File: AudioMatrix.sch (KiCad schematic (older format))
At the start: 124 parts, among them J1 AMP3, J2 AMP1, J3 AMP2, J4 Audio In, J5 3V3, J6 5V, J7 GND, J8 IO, J9 ESP, U1 PT2258, U2 PT2258, U3 PT2258, U4 PCA9555PW, U5 MT8816AE1, U6 ESP32-DEVKITC-32D, U7 TPS60403DBVR

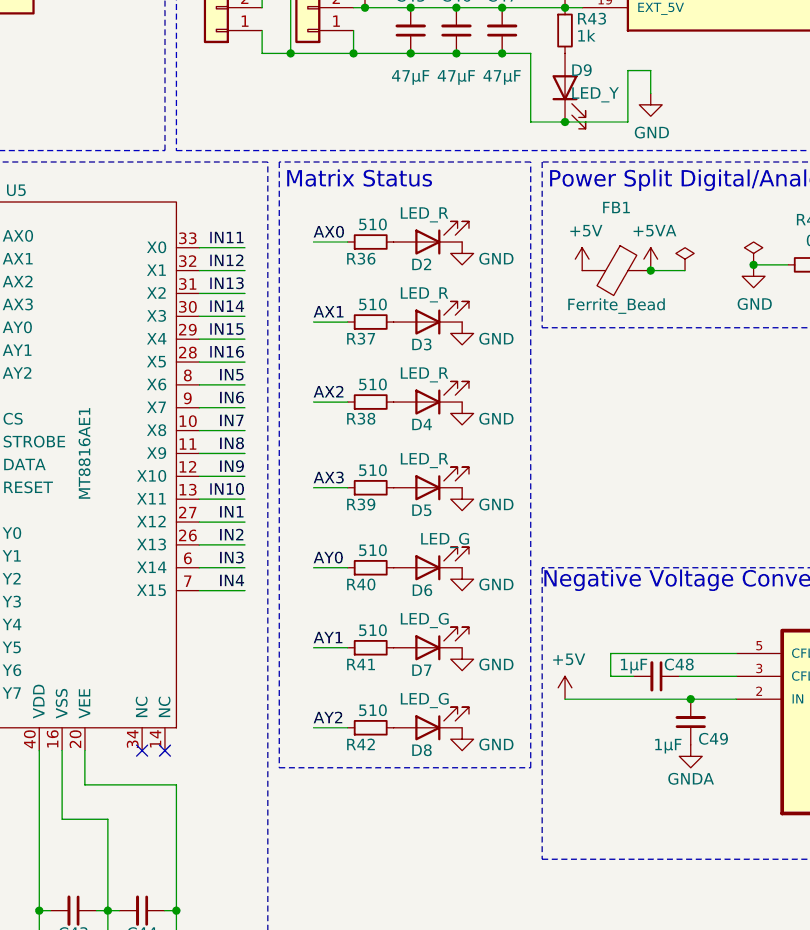
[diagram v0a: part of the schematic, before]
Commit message: Removed LEDs
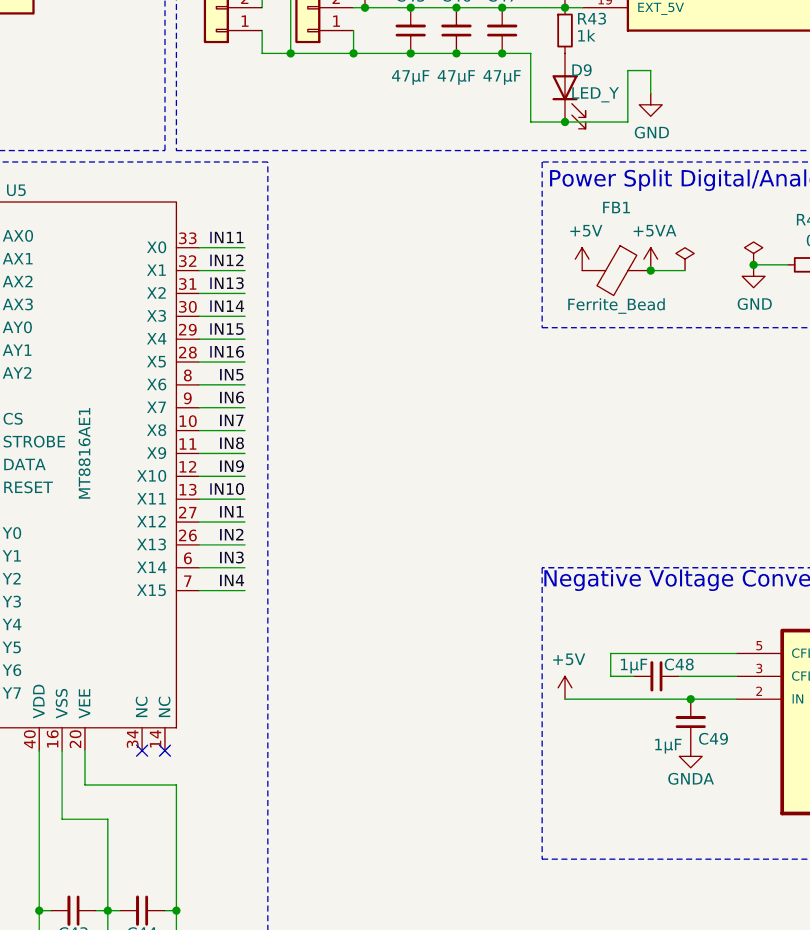
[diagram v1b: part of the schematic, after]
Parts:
- removed D2, D3, D4, D5: LED_R, Diode_SMD:D_0603_1608Metric, symbol Device:LED
- removed D6, D7, D8: LED_G, Diode_SMD:D_0603_1608Metric, symbol Device:LED
- removed R36, R37, R38, R39, R40, R41, R42: 510, Resistor_SMD:R_0603_1608Metric, symbol Device:R_Small
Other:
- note removed: "Matrix Status"

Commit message: Replaced IO expander
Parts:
- removed U4: PCA9555PW, Package_SO:TSSOP-24_4.4x7.8mm_P0.65mm, symbol Interface_Expansion:PCA9555PW
- added R36, R37: 100k, Resistor_SMD:R_0603_1608Metric, symbol Device:R_Small
- added U4: TCA6416APWR, SOP65P640X120-24N, symbol TCA6416APWR:TCA6416APWR
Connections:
- net +5V: now also U4.24 (VCCP)
- net GND: now also C42.2, U4.12 (GND), U4.21 (ADDR); no longer C42.1
- net IO0_0: now also U4.4 (P00)
- net IO0_1: now also U4.5 (P01)
- net IO0_2: now also U4.6 (P02)
- net IO0_3: now also U4.7 (P03)
- net IO0_4: now also U4.8 (P04)
- net IO0_5: now also U4.9 (P05)
- net IO0_6: now also U4.10 (P06)
- net IO0_7: now also U4.11 (P07)
- net IO1_0: now also U4.13 (P10)
- net IO1_1: now also U4.14 (P11)
- net IO1_2: now also U4.15 (P12)
- net IO1_3: now also U4.16 (P13)
- net IO1_4: now also U4.17 (P14)
- net IO1_5: now also U4.18 (P15)
- net IO1_6: now also U4.19 (P16)
- net IO1_7: now also U4.20 (P17)
- net SCL: now also U4.22 (SCL)
- net SDA: now also U4.23 (SDA)
- net 3V3 renamed +3V3
- net +3V3: now also C42.1, R36.1, R37.2, U4.2 (VCC1); no longer C42.2
- new net: R37.1, U4.1 (~INT)
- new net: R36.2, U4.3 (~RESET)
- no-connect marks 15 -> 14
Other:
- moved on the sheet: C42

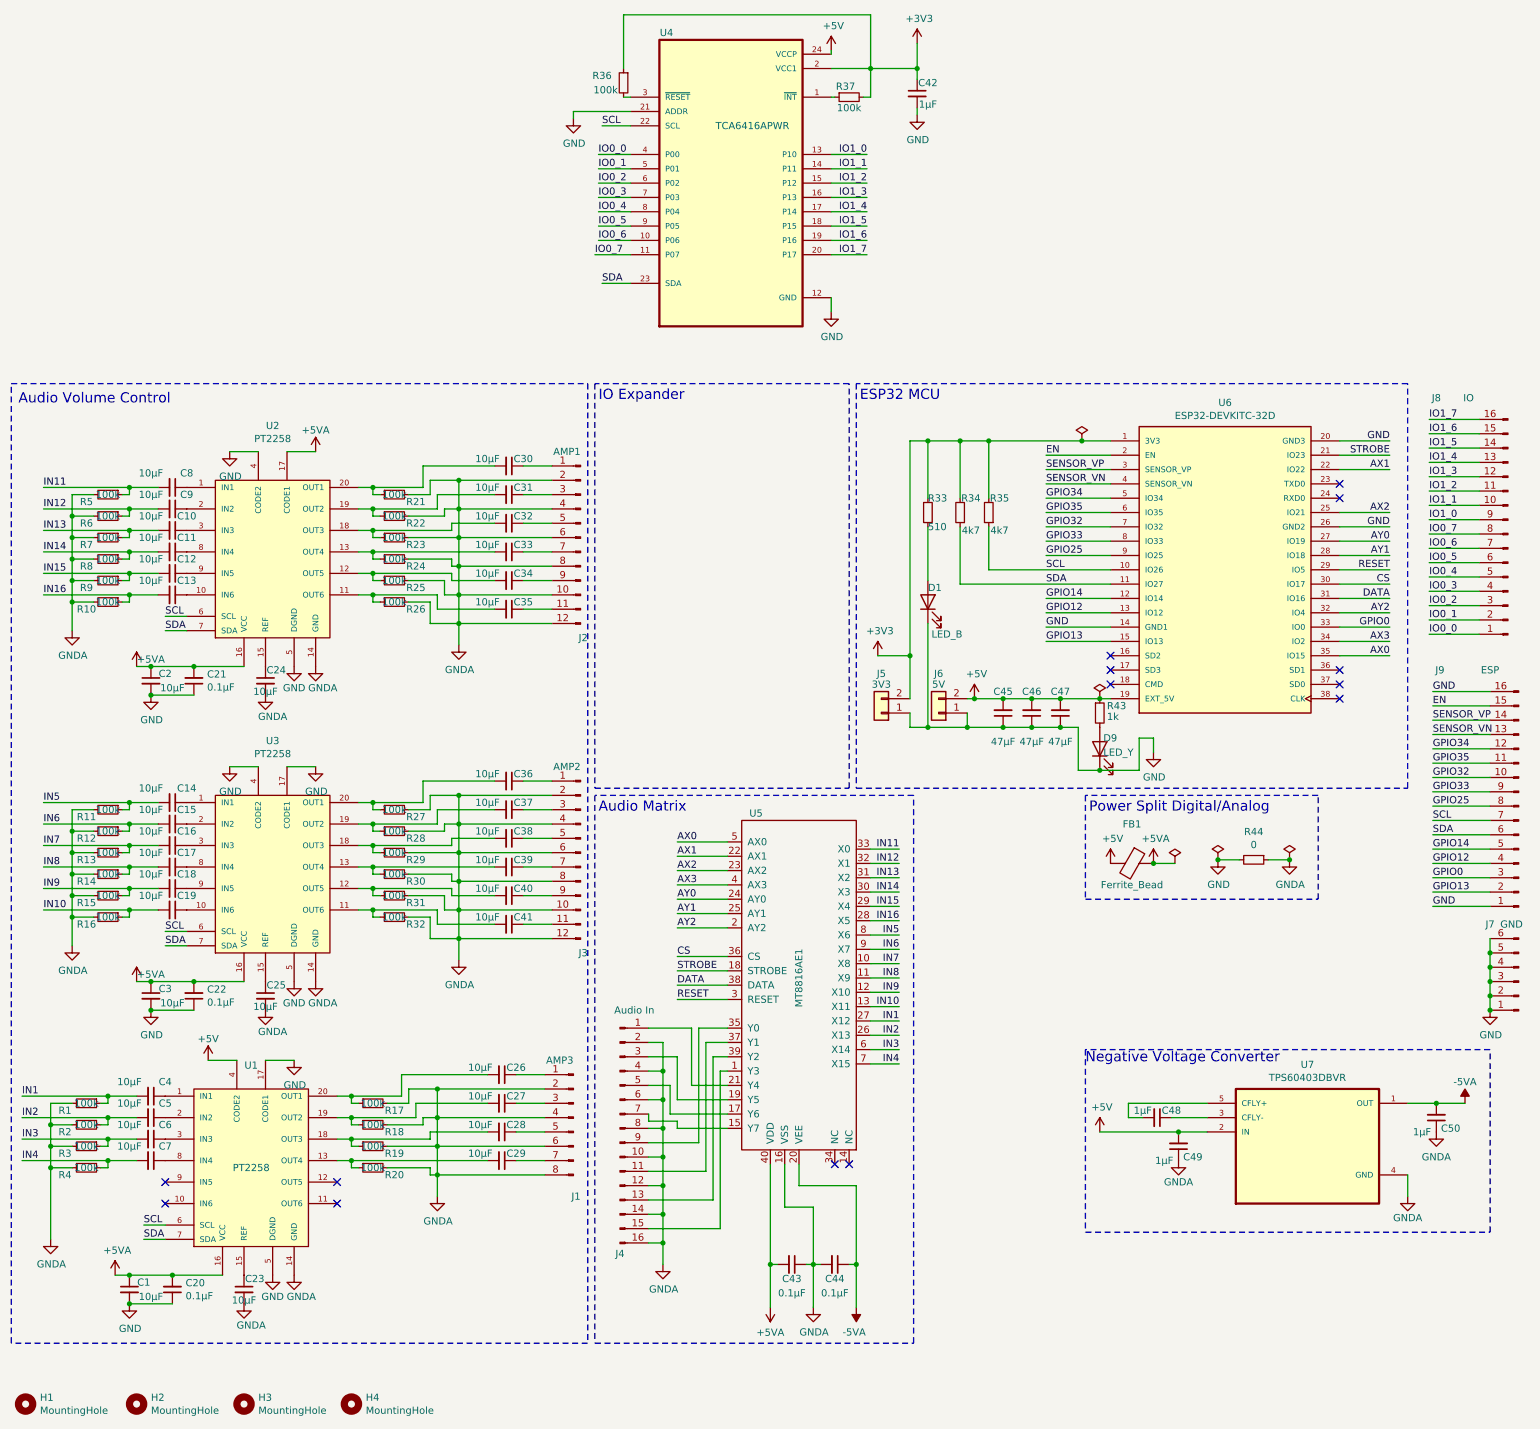
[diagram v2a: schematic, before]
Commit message: Fixed output cap design
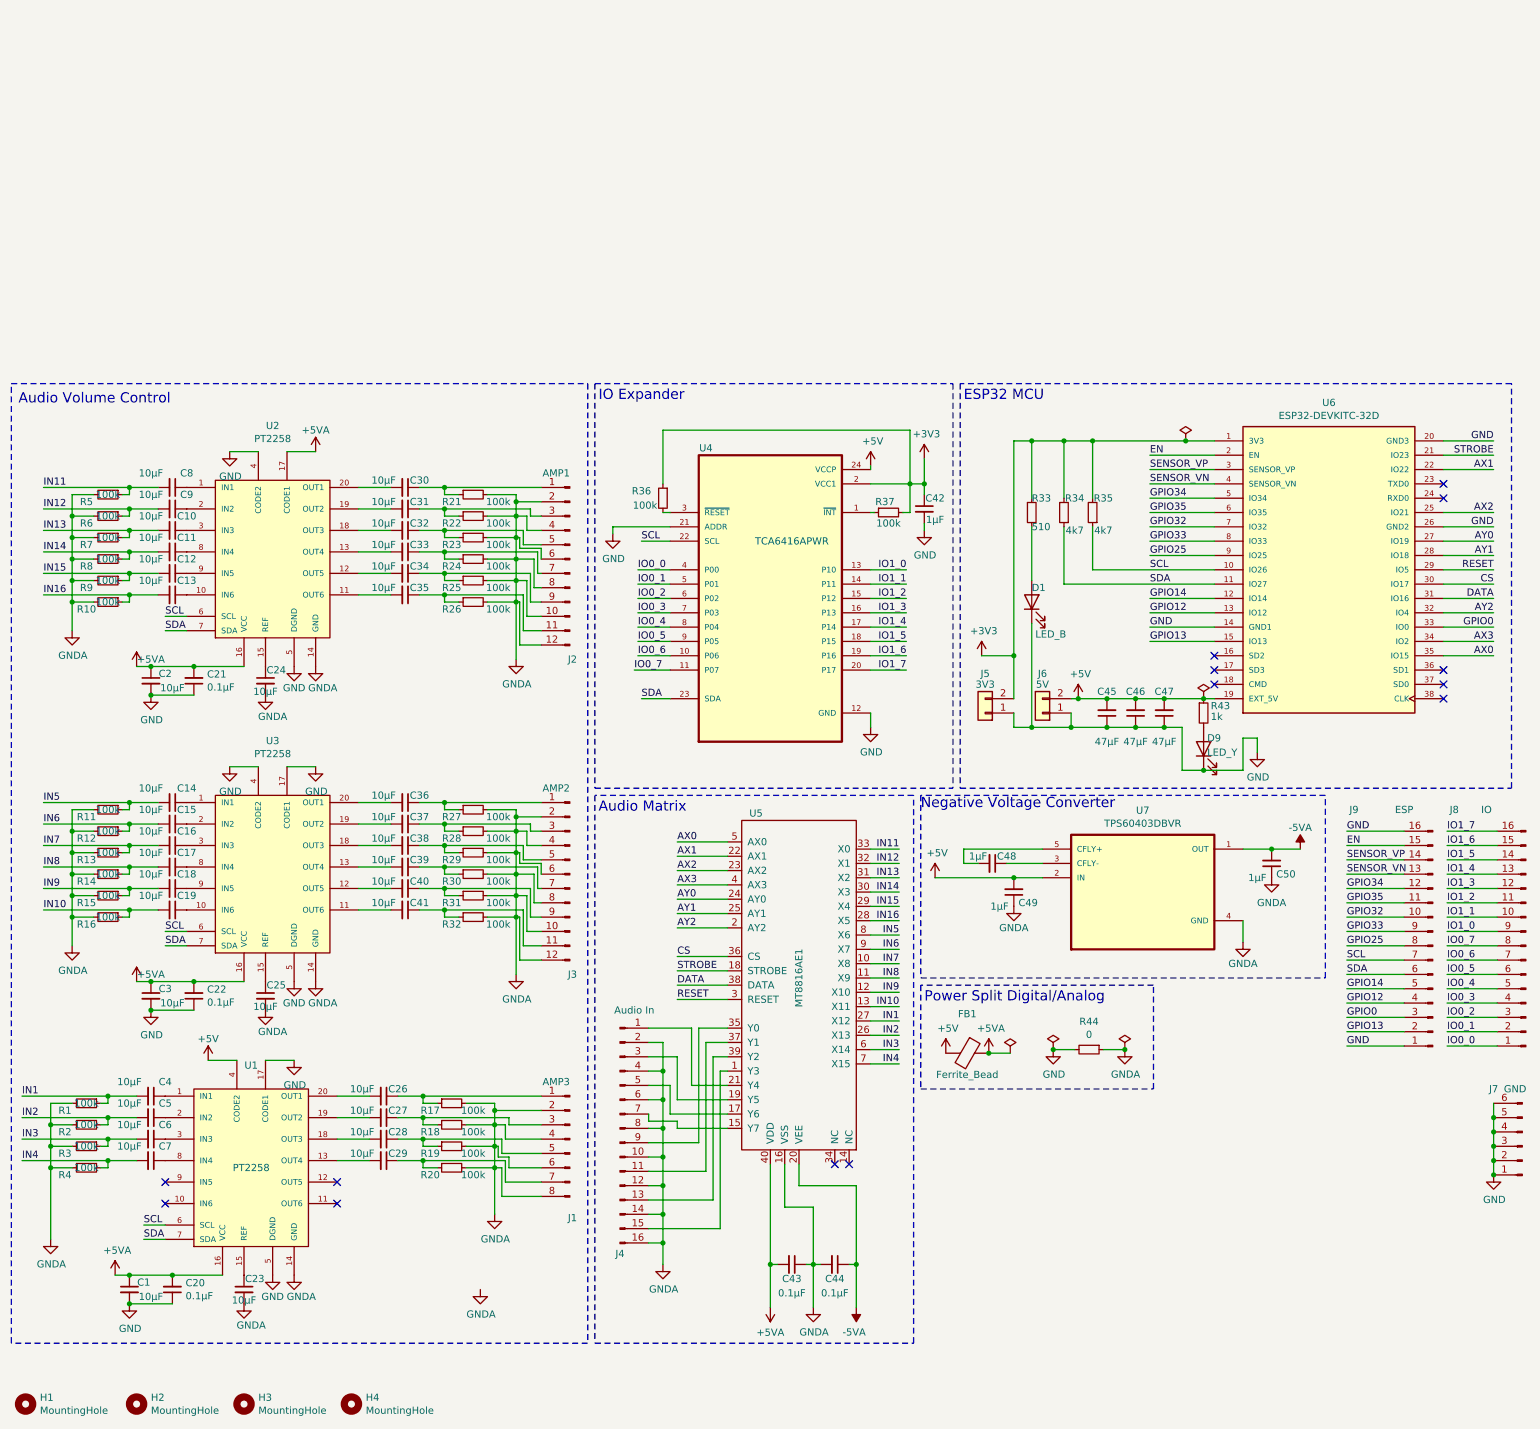
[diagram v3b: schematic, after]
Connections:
- net at C35.2, U2.11 (OUT6): no longer R26.1
- net at C34.2, U2.12 (OUT5): no longer R25.1
- net at C33.2, U2.13 (OUT4): no longer R24.1
- net at C32.2, U2.18 (OUT3): no longer R23.1
- net at C31.2, U2.19 (OUT2): no longer R22.1
- net at C30.2, U2.20 (OUT1): no longer R21.1
- net at C30.1, J2.1 (Pin_1): now also R21.1
- net at C31.1, J2.3 (Pin_3): now also R22.1
- net at C32.1, J2.5 (Pin_5): now also R23.1
- net at C33.1, J2.7 (Pin_7): now also R24.1
- net at C34.1, J2.9 (Pin_9): now also R25.1
- net at C35.1, J2.11 (Pin_11): now also R26.1
- net at C36.1, J3.1 (Pin_1): now also R27.1
- net at C36.2, U3.20 (OUT1): no longer R27.1
- net at C37.1, J3.3 (Pin_3): now also R28.1
- net at C37.2, U3.19 (OUT2): no longer R28.1
- net at C38.1, J3.5 (Pin_5): now also R29.1
- net at C38.2, U3.18 (OUT3): no longer R29.1
- net at C39.1, J3.7 (Pin_7): now also R30.1
- net at C39.2, U3.13 (OUT4): no longer R30.1
- net at C40.1, J3.9 (Pin_9): now also R31.1
- net at C40.2, U3.12 (OUT5): no longer R31.1
- net at C41.1, J3.11 (Pin_11): now also R32.1
- net at C41.2, U3.11 (OUT6): no longer R32.1
- net at C26.1, J1.1 (Pin_1): now also R17.1
- net at C26.2, U1.20 (OUT1): no longer R17.1
- net at C27.1, J1.3 (Pin_3): now also R18.1
- net at C27.2, U1.19 (OUT2): no longer R18.1
- net at C28.1, J1.5 (Pin_5): now also R19.1
- net at C28.2, U1.18 (OUT3): no longer R19.1
- net at C29.1, J1.7 (Pin_7): now also R20.1
- net at C29.2, U1.13 (OUT4): no longer R20.1
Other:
- moved on the sheet: C26, C27, C28, C29, C30, C31, C32, C33, C34, C35, C36, C37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

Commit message: Changed component placement of volume controllers
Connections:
- net GNDA: now also J1.1 (Pin_1), J1.3 (Pin_3), J1.5 (Pin_5), J1.7 (Pin_7), J2.1 (Pin_1), J2.11 (Pin_11), J2.3 (Pin_3), J2.5 (Pin_5), J2.7 (Pin_7), J2.9 (Pin_9), J3.1 (Pin_1), J3.11 (Pin_11), J3.3 (Pin_3), J3.5 (Pin_5), J3.7 (Pin_7), J3.9 (Pin_9); no longer J1.2 (Pin_2), J1.4 (Pin_4), J1.6 (Pin_6), J1.8 (Pin_8), J2.10 (Pin_10), J2.12 (Pin_12), J2.2 (Pin_2), J2.4 (Pin_4), J2.6 (Pin_6), J2.8 (Pin_8), J3.10 (Pin_10), J3.12 (Pin_12), J3.2 (Pin_2), J3.4 (Pin_4), J3.6 (Pin_6), J3.8 (Pin_8)
- net IN1: now also C7.2, R4.1; no longer C4.2, R1.1
- net IN10: now also C14.2, R11.1; no longer C19.2, R16.1
- net IN11: now also C13.2, R10.1; no longer C8.2, R5.1
- net IN12: now also C12.2, R9.1; no longer C9.2, R6.1
- net IN13: now also C11.2, R8.1; no longer C10.2, R7.1
- net IN14: now also C10.2, R7.1; no longer C11.2, R8.1
- net IN15: now also C9.2, R6.1; no longer C12.2, R9.1
- net IN16: now also C8.2, R5.1; no longer C13.2, R10.1
- net IN2: now also C6.2, R3.1; no longer C5.2, R2.1
- net IN3: now also C5.2, R2.1; no longer C6.2, R3.1
- net IN4: now also C4.2, R1.1; no longer C7.2, R4.1
- net IN5: now also C19.2, R16.1; no longer C14.2, R11.1
- net IN6: now also C18.2, R15.1; no longer C15.2, R12.1
- net IN7: now also C17.2, R14.1; no longer C16.2, R13.1
- net IN8: now also C16.2, R13.1; no longer C17.2, R14.1
- net IN9: now also C15.2, R12.1; no longer C18.2, R15.1
- net at C30.1, R21.1: now also J2.12 (Pin_12); no longer J2.1 (Pin_1)
- net at C31.1, R22.1: now also J2.10 (Pin_10); no longer J2.3 (Pin_3)
- net at C32.1, R23.1: now also J2.8 (Pin_8); no longer J2.5 (Pin_5)
- net at C33.1, R24.1: now also J2.6 (Pin_6); no longer J2.7 (Pin_7)
- net at C34.1, R25.1: now also J2.4 (Pin_4); no longer J2.9 (Pin_9)
- net at C35.1, R26.1: now also J2.2 (Pin_2); no longer J2.11 (Pin_11)
- net at C36.1, R27.1: now also J3.12 (Pin_12); no longer J3.1 (Pin_1)
- net at C37.1, R28.1: now also J3.10 (Pin_10); no longer J3.3 (Pin_3)
- net at C38.1, R29.1: now also J3.8 (Pin_8); no longer J3.5 (Pin_5)
- net at C39.1, R30.1: now also J3.6 (Pin_6); no longer J3.7 (Pin_7)
- net at C40.1, R31.1: now also J3.4 (Pin_4); no longer J3.9 (Pin_9)
- net at C41.1, R32.1: now also J3.2 (Pin_2); no longer J3.11 (Pin_11)
- net at C26.1, R17.1: now also J1.8 (Pin_8); no longer J1.1 (Pin_1)
- net at C27.1, R18.1: now also J1.6 (Pin_6); no longer J1.3 (Pin_3)
- net at C28.1, R19.1: now also J1.4 (Pin_4); no longer J1.5 (Pin_5)
- net at C29.1, R20.1: now also J1.2 (Pin_2); no longer J1.7 (Pin_7)
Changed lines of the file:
@@
 Wire Wire Line
 	750  2000 1350 2000
-Text Label 750  3450 0    50   ~ 0
+Text Label 750  4200 0    50   ~ 0
 IN5
-Text Label 750  3600 0    50   ~ 0
+Text Label 750  4050 0    50   ~ 0
 IN6
 Text Label 1600 4350 0    50   ~ 0
@@
 L Connector:Conn_01x12_Male J3
 U 1 1 61857BD2
-P 4425 3950
-F 0 "J3" H 4375 3250 50  0000 L CNN
-F 1 "AMP2" H 4425 4550 50  0000 L CNN
-F 2 "Connector_PinHeader_2.54mm:PinHeader_1x12_P2.54mm_Vertical" H 4425 3950 50  0001 C CNN
-F 3 "~" H 4425 3950 50  0001 C CNN
-	1    4425 3950
-	-1   0    0    -1
+P 4425 4050
+F 0 "J3" H 4375 3350 50  0000 L CNN
+F 1 "AMP2" H 4425 4650 50  0000 L CNN
+F 2 "Connector_PinHeader_2.54mm:PinHeader_1x12_P2.54mm_Vertical" H 4425 4050 50  0001 C CNN
+F 3 "~" H 4425 4050 50  0001 C CNN
+	1    4425 4050
+	-1   0    0    1
 $EndComp
 Wire Wire Line
@@
 Wire Wire Line
 	750  4200 1350 4200
+Text Label 750  3900 0    50   ~ 0
+IN7
 Text Label 750  3750 0    50   ~ 0
-IN7
-Text Label 750  3900 0    50   ~ 0
 IN8
-Text Label 750  4050 0    50   ~ 0
+Text Label 750  3600 0    50   ~ 0
 IN9
-Text Label 750  4200 0    50   ~ 0
+Text Label 750  3450 0    50   ~ 0
 IN10
-Text Label 750  1250 0    50   ~ 0
+Text Label 750  2000 0    50   ~ 0
 IN11
-Text Label 750  1400 0    50   ~ 0
+Text Label 750  1850 0    50   ~ 0
 IN12
 Text Label 1450 6400 0    50   ~ 0
@@
 Wire Wire Line
 	600  5950 1200 5950
+Text Label 750  1700 0    50   ~ 0
+IN13
 Text Label 750  1550 0    50   ~ 0
-IN13
-Text Label 750  1700 0    50   ~ 0
 IN14
-Text Label 750  1850 0    50   ~ 0
+Text Label 750  1400 0    50   ~ 0
 IN15
-Text Label 750  2000 0    50   ~ 0
+Text Label 750  1250 0    50   ~ 0
 IN16
 Wire Wire Line
@@
 Connection ~ 1350 1400
 Connection ~ 1350 1250
+Text Label 600  5500 0    50   ~ 0
+IN4
+Text Label 600  5650 0    50   ~ 0
+IN3
+Text Label 600  5800 0    50   ~ 0
+IN2
 Text Label 600  5950 0    50   ~ 0
-IN4
-Text Label 600  5800 0    50   ~ 0
-IN3
-Text Label 600  5650 0    50   ~ 0
-IN2
-Text Label 600  5500 0    50   ~ 0
 IN1
 Wire Wire Line
@@
 L Connector:Conn_01x12_Male J2
 U 1 1 60CE6482
-P 4425 1750
-F 0 "J2" H 4375 1050 50  0000 L CNN
-F 1 "AMP1" H 4425 2350 50  0000 L CNN
-F 2 "Connector_PinHeader_2.54mm:PinHeader_1x12_P2.54mm_Vertical" H 4425 1750 50  0001 C CNN
-F 3 "~" H 4425 1750 50  0001 C CNN
-	1    4425 1750
-	-1   0    0    -1
-$EndComp
-$Comp
-L power:GNDA #PWR?
+P 4425 1850
+F 0 "J2" H 4375 1150 50  0000 L CNN
+F 1 "AMP1" H 4425 2450 50  0000 L CNN
+F 2 "Connector_PinHeader_2.54mm:PinHeader_1x12_P2.54mm_Vertical" H 4425 1850 50  0001 C CNN
+F 3 "~" H 4425 1850 50  0001 C CNN
+	1    4425 1850
+	-1   0    0    1
+$EndComp
+$Comp
+L power:GNDA #PWR0105
 U 1 1 637AE914
 P 4050 4650
-F 0 "#PWR?" H 4050 4400 50  0001 C CNN
+F 0 "#PWR0105" H 4050 4400 50  0001 C CNN
 F 1 "GNDA" H 4055 4477 50  0000 C CNN
 F 2 "" H 4050 4650 50  0001 C CNN
@@
 	4225 3875 4225 3950
 $Comp
-L power:GNDA #PWR?
+L power:GNDA #PWR0106
 U 1 1 63B33A15
 P 3900 6325
-F 0 "#PWR?" H 3900 6075 50  0001 C CNN
+F 0 "#PWR0106" H 3900 6075 50  0001 C CNN
 F 1 "GNDA" H 3905 6152 50  0000 C CNN
 F 2 "" H 3900 6325 50  0001 C CNN
@@
 Wire Wire Line
 	3400 6000 3500 6000
-$Comp
-L Connector:Conn_01x08_Male J1
-U 1 1 618853C0
-P 4425 5800
-F 0 "J1" H 4375 5250 50  0000 L CNN
-F 1 "AMP3" H 4425 6200 50  0000 L CNN
-F 2 "Connector_PinHeader_2.54mm:PinHeader_1x08_P2.54mm_Vertical" H 4425 5800 50  0001 C CNN
-F 3 "~" H 4425 5800 50  0001 C CNN
-	1    4425 5800
-	-1   0    0    -1
-$EndComp
 Wire Wire Line
 	3400 5500 4225 5500
-Wire Wire Line
-	3900 5600 4225 5600
 Wire Wire Line
 	4000 5700 4225 5700
@@
 Wire Notes Line
 	7100 525  7100 3350
+Wire Wire Line
+	3900 5600 4225 5600
+$Comp
+L Connector:Conn_01x08_Male J1
+U 1 1 618853C0
+P 4425 5900
+F 0 "J1" H 4375 5350 50  0000 L CNN
+F 1 "AMP3" H 4425 6300 50  0000 L CNN
+F 2 "Connector_PinHeader_2.54mm:PinHeader_1x08_P2.54mm_Vertical" H 4425 5900 50  0001 C CNN
+F 3 "~" H 4425 5900 50  0001 C CNN
+	1    4425 5900
+	-1   0    0    1
+$EndComp
 $EndSCHEMATC

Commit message: Net labeling and cleanup
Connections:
- net AX1: now also U6.25 (IO21); no longer U6.22 (IO22)
- net AX2: now also U6.27 (IO19); no longer U6.25 (IO21)
- net AY0: now also U6.28 (IO18); no longer U6.27 (IO19)
- net AY1: now also U6.29 (IO5); no longer U6.28 (IO18)
- net AY2: now also U6.33 (IO0); no longer U6.32 (IO4)
- net CS: now also U6.31 (IO16); no longer U6.30 (IO17)
- net DATA: now also U6.32 (IO4); no longer U6.31 (IO16)
- net RESET: now also U6.30 (IO17); no longer U6.29 (IO5)
- net GPIO0 renamed GPIO22
- net GPIO22: now also U6.22 (IO22); no longer U6.33 (IO0)
- net IN1 renamed X12
- net IN10 renamed X11
- net IN11 renamed X0
- net IN12 renamed X1
- net IN13 renamed X2
- net IN14 renamed X3
- net IN15 renamed X4
- net IN16 renamed X5
- net IN2 renamed X13
- net IN3 renamed X14
- net IN4 renamed X15
- net IN5 renamed X6
- net IN6 renamed X7
- net IN7 renamed X8
- net IN8 renamed X9
- net IN9 renamed X10
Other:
- note added: "License: CERN-OHL-W Version 2"
- moved on the sheet: C1, C20, C23, C26, C27, C28, C29, C4, C5, C6, C7, R1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
